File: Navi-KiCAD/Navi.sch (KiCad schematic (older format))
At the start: 30 parts, among them U10 Logo, U11 Logo, U6 LP5521YQ/NOPB

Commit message: Some BOM consolidation.
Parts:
- R40, R41: value DNP -> 0 DNP
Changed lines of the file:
@@
 U 1 1 58D60CF9
 P 2400 4400
-F 0 "R40" V 2450 4250 50  0000 C CNN
-F 1 "DNP" V 2400 4400 50  0000 C CNN
+F 0 "R40" V 2400 4400 50  0000 C CNN
+F 1 "0 DNP" V 2350 4150 50  0000 C CNN
 F 2 "Resistors_SMD:R_0402" V -5050 2750 50  0001 C CNN
 F 3 "" V -4770 2750 50  0001 C CNN
@@
 U 1 1 58D60FCF
 P 3450 4400
-F 0 "R41" V 3500 4600 50  0000 C CNN
-F 1 "DNP" V 3450 4400 50  0000 C CNN
+F 0 "R41" V 3450 4400 50  0000 C CNN
+F 1 "0 DNP" V 3500 4650 50  0000 C CNN
 F 2 "Resistors_SMD:R_0402" V -4000 2750 50  0001 C CNN
 F 3 "" V -3720 2750 50  0001 C CNN

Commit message: Completed key routing.
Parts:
- renumbered C91 to C1, C92 to C2, C93 to C3, C94 to C4, D3 to D1, D4 to D2, D8 to D3, R39 to R1, R28 to R10, R29 to R11, R30 to R12, R31 to R13, R32 to R14, R33 to R15, R34 to R16, R40 to R2, R24 to R3, R25 to R4, R26 to R5, R41 to R6, R45 to R7, R27 to R8, R49 to R9, U6 to U1, U10 to U2, U11 to U3
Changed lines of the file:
@@
 CPU-SDA
 $Comp
-L R R27
+L R R8
 U 1 1 58BFD165
 P 6400 2050
-F 0 "R27" H 6470 2149 50  0000 L CNN
+F 0 "R8" H 6470 2149 50  0000 L CNN
 F 1 "1k" H 6470 2058 50  0000 L CNN
 F 2 "Resistors_SMD:R_0402" V -1050 400 50  0001 C CNN
@@
 $EndComp
 $Comp
-L R R28
+L R R10
 U 1 1 58BFD565
 P 6650 2050
-F 0 "R28" H 6720 2149 50  0000 L CNN
+F 0 "R10" H 6720 2149 50  0000 L CNN
 F 1 "1k" H 6720 2058 50  0000 L CNN
 F 2 "Resistors_SMD:R_0402" V -800 400 50  0001 C CNN
@@
 $EndComp
 $Comp
-L R R26
+L R R5
 U 1 1 58C0DD41
 P 3400 4050
-F 0 "R26" V 3450 3850 50  0000 C CNN
+F 0 "R5" V 3450 3850 50  0000 C CNN
 F 1 "1k" V 3400 4050 50  0000 C CNN
 F 2 "Resistors_SMD:R_0402" V -4050 2400 50  0001 C CNN
@@
 $EndComp
 $Comp
-L R R25
+L R R4
 U 1 1 58C11226
 P 3400 3950
-F 0 "R25" V 3450 3750 50  0000 C CNN
+F 0 "R4" V 3450 3750 50  0000 C CNN
 F 1 "1k" V 3400 3950 50  0000 C CNN
 F 2 "Resistors_SMD:R_0402" V -4050 2300 50  0001 C CNN
@@
 $EndComp
 $Comp
-L R R24
+L R R3
 U 1 1 58C113C8
 P 3400 3850
-F 0 "R24" V 3450 3650 50  0000 C CNN
+F 0 "R3" V 3450 3650 50  0000 C CNN
 F 1 "1k" V 3400 3850 50  0000 C CNN
 F 2 "Resistors_SMD:R_0402" V -4050 2200 50  0001 C CNN
@@
 100k-PU
 $Comp
-L R R34
+L R R16
 U 1 1 58C4A4F7
 P 7850 4900
-F 0 "R34" V 7900 4700 50  0000 C CNN
+F 0 "R16" V 7900 4700 50  0000 C CNN
 F 1 "1k" V 7850 4900 50  0000 C CNN
 F 2 "Resistors_SMD:R_0402" V 400 3250 50  0001 C CNN
@@
 $EndComp
 $Comp
-L R R33
+L R R15
 U 1 1 58C4A502
 P 7850 4800
-F 0 "R33" V 7900 4600 50  0000 C CNN
+F 0 "R15" V 7900 4600 50  0000 C CNN
 F 1 "1k" V 7850 4800 50  0000 C CNN
 F 2 "Resistors_SMD:R_0402" V 400 3150 50  0001 C CNN
@@
 $EndComp
 $Comp
-L R R32
+L R R14
 U 1 1 58C4A50D
 P 7850 4700
-F 0 "R32" V 7900 4500 50  0000 C CNN
+F 0 "R14" V 7900 4500 50  0000 C CNN
 F 1 "1k" V 7850 4700 50  0000 C CNN
 F 2 "Resistors_SMD:R_0402" V 400 3050 50  0001 C CNN
@@
 100k-PU
 $Comp
-L R R31
+L R R13
 U 1 1 58C89A2C
 P 7850 3200
-F 0 "R31" V 7900 3000 50  0000 C CNN
+F 0 "R13" V 7900 3000 50  0000 C CNN
 F 1 "1k" V 7850 3200 50  0000 C CNN
 F 2 "Resistors_SMD:R_0402" V 400 1550 50  0001 C CNN
@@
 $EndComp
 $Comp
-L R R30
+L R R12
 U 1 1 58C89A37
 P 7850 3100
-F 0 "R30" V 7900 2900 50  0000 C CNN
+F 0 "R12" V 7900 2900 50  0000 C CNN
 F 1 "1k" V 7850 3100 50  0000 C CNN
 F 2 "Resistors_SMD:R_0402" V 400 1450 50  0001 C CNN
@@
 $EndComp
 $Comp
-L R R29
+L R R11
 U 1 1 58C89A42
 P 7850 3000
-F 0 "R29" V 7900 2800 50  0000 C CNN
+F 0 "R11" V 7900 2800 50  0000 C CNN
 F 1 "1k" V 7850 3000 50  0000 C CNN
 F 2 "Resistors_SMD:R_0402" V 400 1350 50  0001 C CNN
@@
 PD[0..11]
 $Comp
-L R R45
+L R R7
 U 1 1 58C46FCA
 P 5850 6700
-F 0 "R45" H 5920 6799 50  0000 L CNN
+F 0 "R7" H 5920 6799 50  0000 L CNN
 F 1 "10k" H 5920 6708 50  0000 L CNN
 F 2 "Resistors_SMD:R_0402" V -1600 5050 50  0001 C CNN
@@
 	5850 6950 5850 6850
 $Comp
-L LED D4
+L LED D2
 U 1 1 58C46FD1
 P 5850 7100
-F 0 "D4" V 5950 7050 50  0000 R CNN
+F 0 "D2" V 5950 7050 50  0000 R CNN
 F 1 "MF-LED-0603-GREEN" H 6100 7200 50  0000 R CNN
 F 2 "LEDs:LED_0603" H 450 750 50  0001 C CNN
@@
 $EndComp
 $Comp
-L LED D8
+L LED D3
 U 1 1 58C4B3ED
 P 6550 7100
-F 0 "D8" V 6650 7050 50  0000 R CNN
+F 0 "D3" V 6650 7050 50  0000 R CNN
 F 1 "MF-LED-0603-GREEN" H 6800 7200 50  0000 R CNN
 F 2 "LEDs:LED_0603" H 1150 750 50  0001 C CNN
@@
 $EndComp
 $Comp
-L R R49
+L R R9
 U 1 1 58C4B93C
 P 6550 6700
-F 0 "R49" H 6620 6799 50  0000 L CNN
+F 0 "R9" H 6620 6799 50  0000 L CNN
 F 1 "10k" H 6620 6708 50  0000 L CNN
 F 2 "Resistors_SMD:R_0402" V -900 5050 50  0001 C CNN
@@
 $EndComp
 $Comp
-L LED_BGR D3
+L LED_BGR D1
 U 1 1 58C9F1F2
 P 4850 6900
-F 0 "D3" V 4896 6570 50  0000 R CNN
+F 0 "D1" V 4896 6570 50  0000 R CNN
 F 1 "CLX6D-FKB-CMPQSGKBB7A363" H 5200 7300 50  0000 R CNN
 F 2 "LEDs:LED_PLCC6_3.4x3.4mm" H 200 150 50  0001 C CNN
@@
 $EndComp
 $Comp
-L C C91
+L C C1
 U 1 1 58CB9DB2
 P 1700 5650
-F 0 "C91" H 1750 5750 50  0000 L CNN
+F 0 "C1" H 1750 5750 50  0000 L CNN
 F 1 "1u" H 1750 5550 50  0000 L CNN
 F 2 "Capacitors_SMD:C_0402" H -4812 4350 50  0001 C CNN
@@
 $EndComp
 $Comp
-L C C94
+L C C4
 U 1 1 58CBBFFD
 P 3800 5650
-F 0 "C94" H 3850 5750 50  0000 L CNN
+F 0 "C4" H 3850 5750 50  0000 L CNN
 F 1 "1u" H 3850 5550 50  0000 L CNN
 F 2 "Capacitors_SMD:C_0402" H -2712 4350 50  0001 C CNN
@@
 	3450 5500 3800 5500
 $Comp
-L C C92
+L C C2
 U 1 1 58CBE629
 P 2500 5350
-F 0 "C92" V 2550 5450 50  0000 L CNN
+F 0 "C2" V 2550 5450 50  0000 L CNN
 F 1 "GRM155R61C474KE01D" V 2650 5100 50  0000 L CNN
 F 2 "Capacitors_SMD:C_0402" H -4012 4050 50  0001 C CNN
@@
 $EndComp
 $Comp
-L C C93
+L C C3
 U 1 1 58CBEC69
 P 3100 5350
-F 0 "C93" V 3150 5450 50  0000 L CNN
+F 0 "C3" V 3150 5450 50  0000 L CNN
 F 1 "GRM155R61C474KE01D" V 3250 4700 50  0000 L CNN
 F 2 "Capacitors_SMD:C_0402" H -3412 4050 50  0001 C CNN
@@
 	1200 5800 1200 6150
 $Comp
-L R R39
+L R R1
 U 1 1 58CCCAB3
 P 1200 5650
-F 0 "R39" H 1270 5749 50  0000 L CNN
+F 0 "R1" H 1270 5749 50  0000 L CNN
 F 1 "10k" H 1270 5658 50  0000 L CNN
 F 2 "Resistors_SMD:R_0402" V -6250 4000 50  0001 C CNN
@@
 	7050 4050 7550 4050
 $Comp
-L R R40
+L R R2
 U 1 1 58D60CF9
 P 2400 4400
-F 0 "R40" V 2400 4400 50  0000 C CNN
+F 0 "R2" V 2400 4400 50  0000 C CNN
 F 1 "0 DNP" V 2350 4150 50  0000 C CNN
 F 2 "Resistors_SMD:R_0402" V -5050 2750 50  0001 C CNN
@@
 $EndComp
 $Comp
-L R R41
+L R R6
 U 1 1 58D60FCF
 P 3450 4400
-F 0 "R41" V 3450 4400 50  0000 C CNN
+F 0 "R6" V 3450 4400 50  0000 C CNN
 F 1 "0 DNP" V 3500 4650 50  0000 C CNN
 F 2 "Resistors_SMD:R_0402" V -4000 2750 50  0001 C CNN
@@
 CPU-SDA
 $Comp
-L BOX1 U11
+L BOX1 U3
 U 1 1 58D75525
 P 7900 6300
-F 0 "U11" H 7950 6350 50  0001 C CNN
+F 0 "U3" H 7950 6350 50  0001 C CNN
 F 1 "Logo" H 8028 6300 50  0000 L CNN
 F 2 "Symbols:NaviLOGO" H 1550 850 60  0001 C CNN
@@
 $EndComp
 $Comp
-L BOX1 U10
+L BOX1 U2
 U 1 1 58D772A7
 P 7900 6150
-F 0 "U10" H 7950 6200 50  0001 C CNN
+F 0 "U2" H 7950 6200 50  0001 C CNN
 F 1 "Logo" H 8028 6150 50  0000 L CNN
 F 2 "Symbols:NaviLOGO" H 1550 700 60  0001 C CNN
@@
 $EndComp
 $Comp
-L LP5521YQ U6
+L LP5521YQ U1
 U 1 1 58D0B021
 P 2800 6450
-F 0 "U6" H 2100 5650 60  0000 C CNN
+F 0 "U1" H 2100 5650 60  0000 C CNN
 F 1 "LP5521YQ/NOPB" H 3250 5650 60  0000 C CNN
 F 2 "Housings_DFN_QFN:QFN-24-1EP_4x5mm_Pitch0.5mm" H -150 -800 60  0001 C CNN

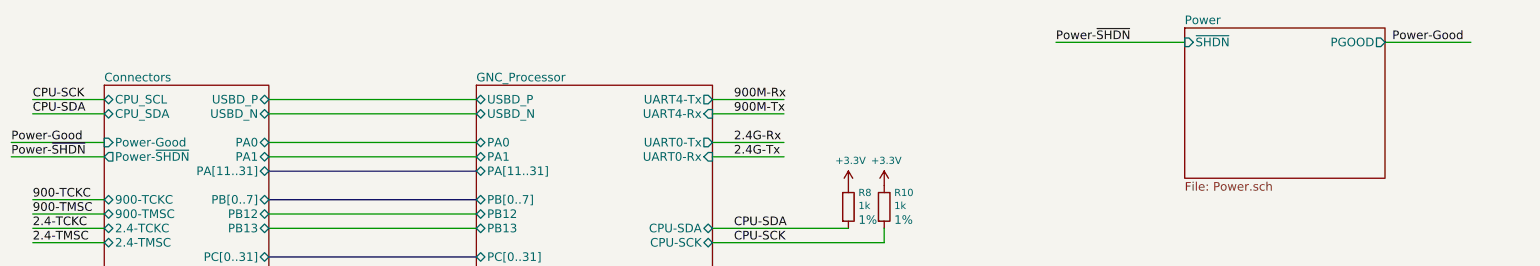
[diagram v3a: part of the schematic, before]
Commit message: Additional routing
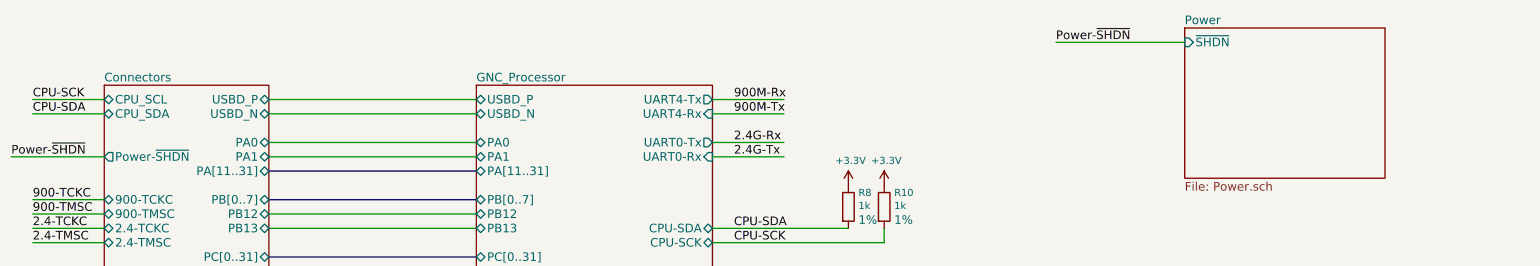
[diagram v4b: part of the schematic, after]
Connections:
- net labels removed: Power-Good
- wire segments 119 -> 117
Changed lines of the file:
@@
 F1 "Power.sch" 60
 F2 "~SHDN" I L 8750 900 60
-F3 "PGOOD" O R 10150 900 60
 $EndSheet
 $Sheet
@@
 F29 "2.4-DIO-[7..22]" B R 2350 3400 60
 F30 "2.4-ADIO-[23..30]" B R 2350 3500 60
-F31 "Power-Good" I L 1200 1600 60
-F32 "Power-~SHDN" O L 1200 1700 60
+F31 "Power-~SHDN" O L 1200 1700 60
 $EndSheet
 Text Label 5600 1600 0    60   ~ 0
@@
 Power-~SHDN~
 Wire Wire Line
-	10150 900  10750 900
-Text Label 10200 900  0    60   ~ 0
-Power-Good
-Wire Wire Line
 	1200 1700 550  1700
 Text Label 550  1700 0    60   ~ 0
 Power-~SHDN~
 Wire Wire Line
-	550  1600 1200 1600
-Text Label 550  1600 0    60   ~ 0
-Power-Good
-Wire Wire Line
 	3800 2900 2350 2900

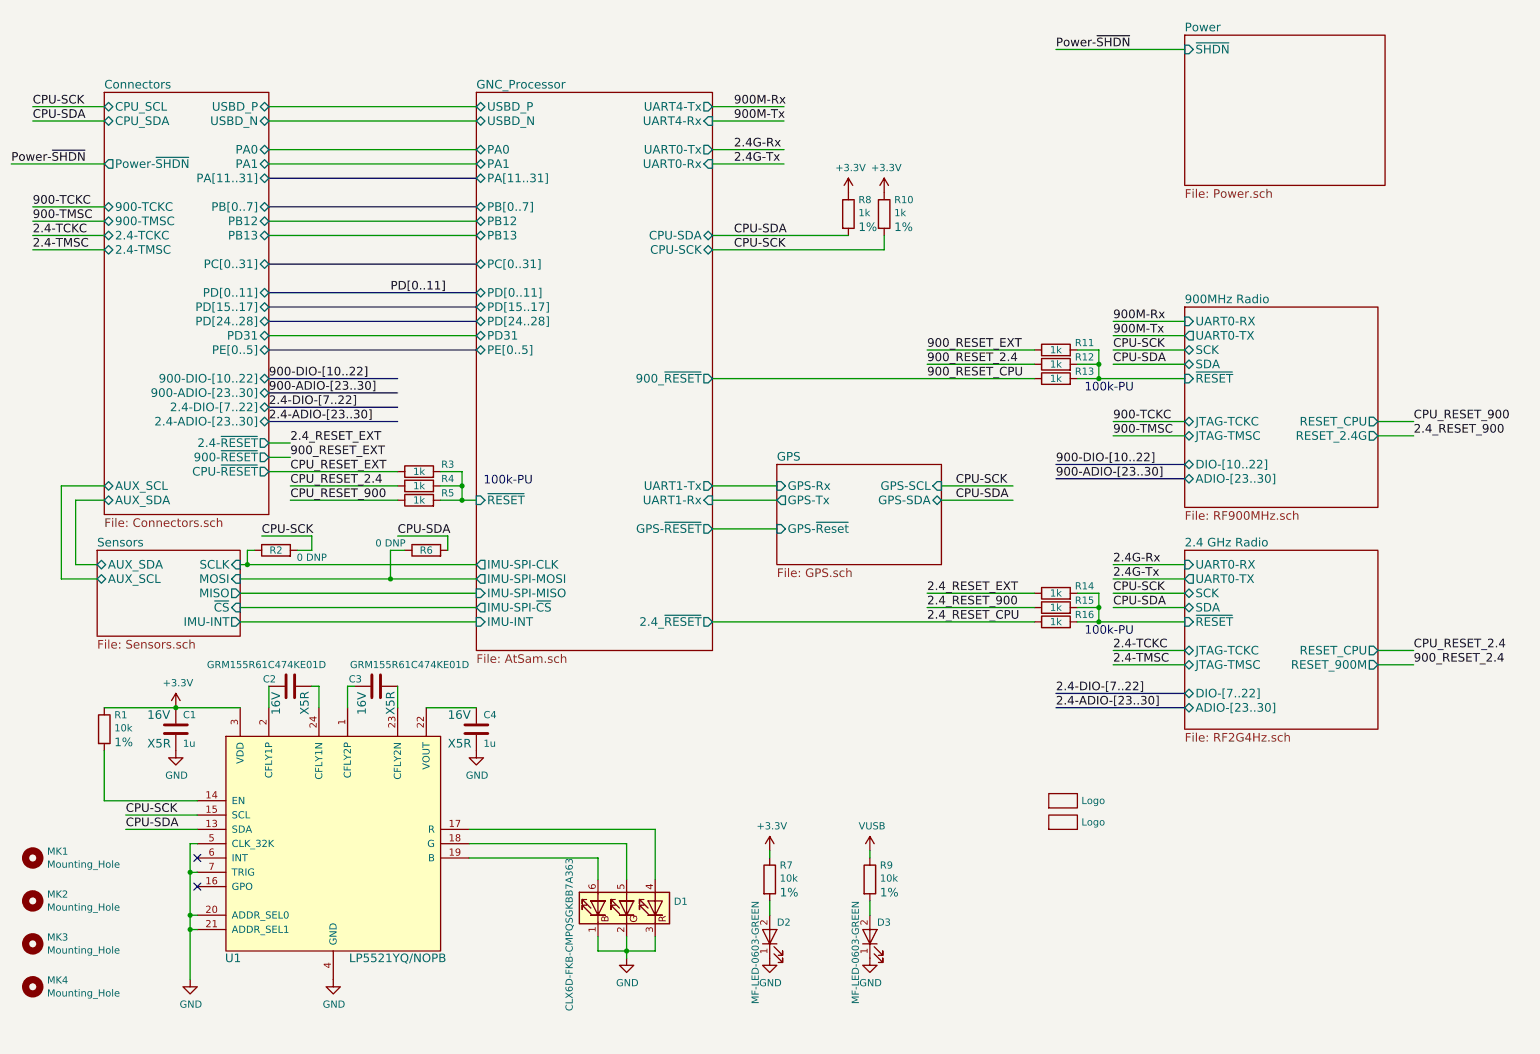
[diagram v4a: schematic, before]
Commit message: Upgraded to 9 channel RGB driver. Broke out signals for LSM303 and LSM6DS3
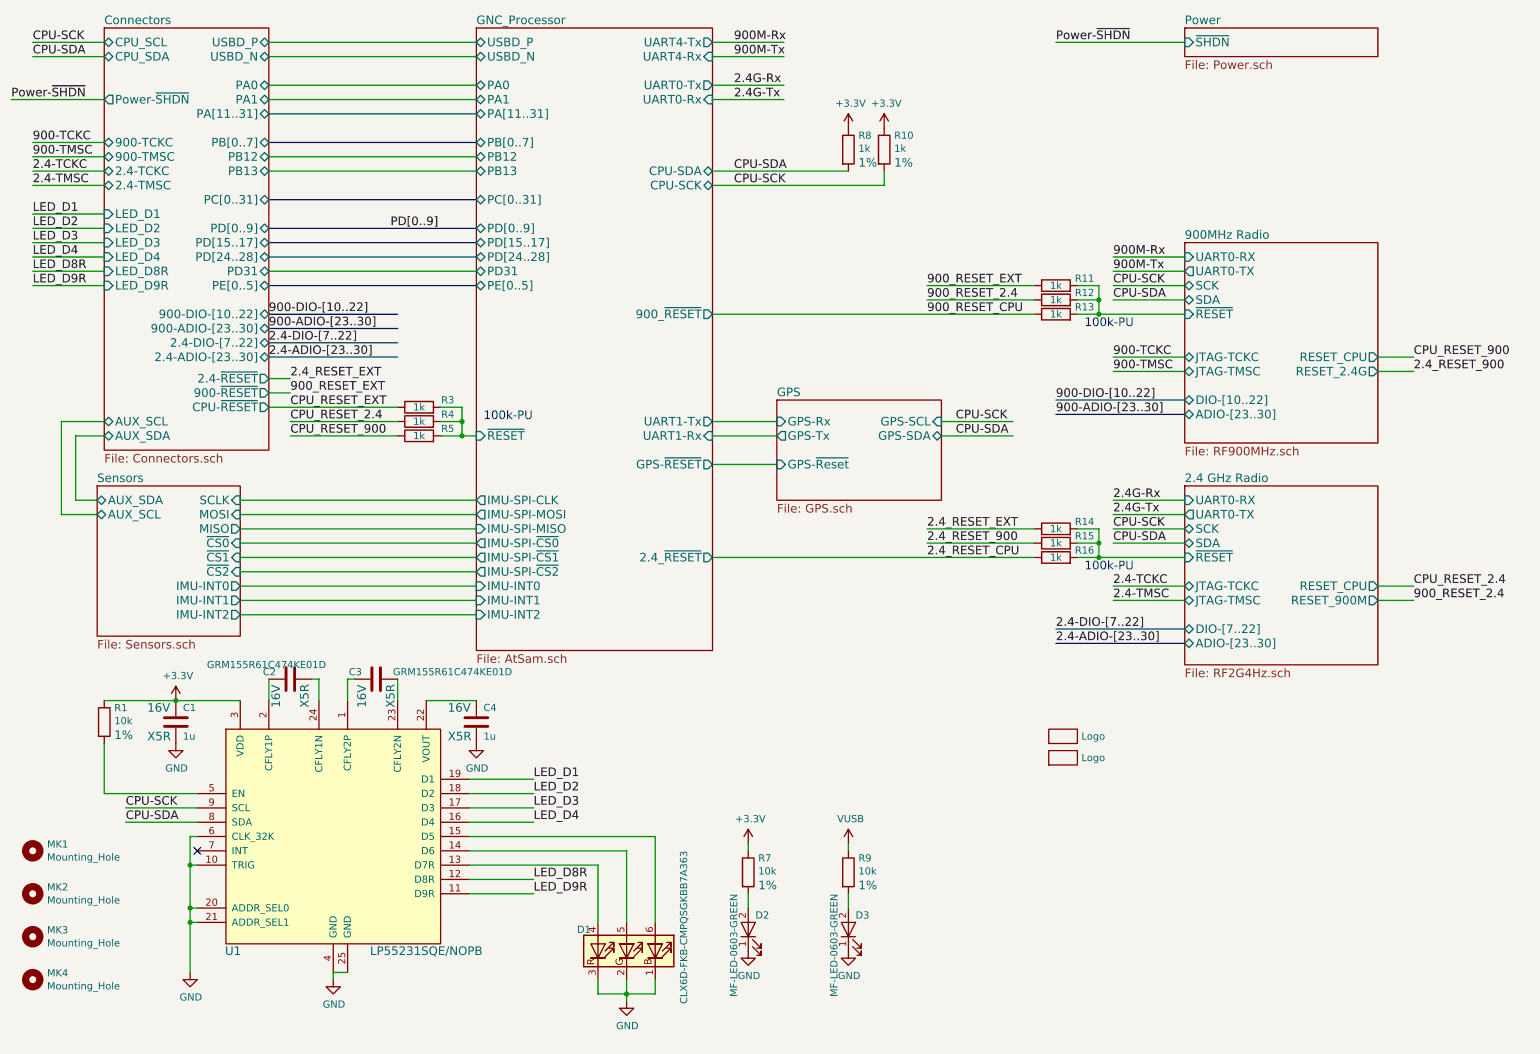
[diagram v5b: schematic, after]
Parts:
- removed R2, R6: 0 DNP, Resistors_SMD:R_0402, symbol R
- removed U1: LP5521YQ/NOPB, Housings_DFN_QFN:QFN-24-1EP_4x5mm_Pitch0.5mm, symbol LP5521YQ
- added U1: LP55231SQE/NOPB, Housings_DFN_QFN:QFN-24-1EP_4x4mm_Pitch0.5mm, symbol LP55231SQE/NOPB
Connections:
- net labels added: LED_D1, LED_D2, LED_D3, LED_D4, LED_D8R, LED_D9R, PD[0..9]
- net labels removed: PD[0..11]
- wire segments 117 -> 126
- no-connect marks 2 -> 1
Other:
- moved on the sheet: C1, C2, C3, C4, D1, D2, D3, MK1, MK2, MK3, MK4, R1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

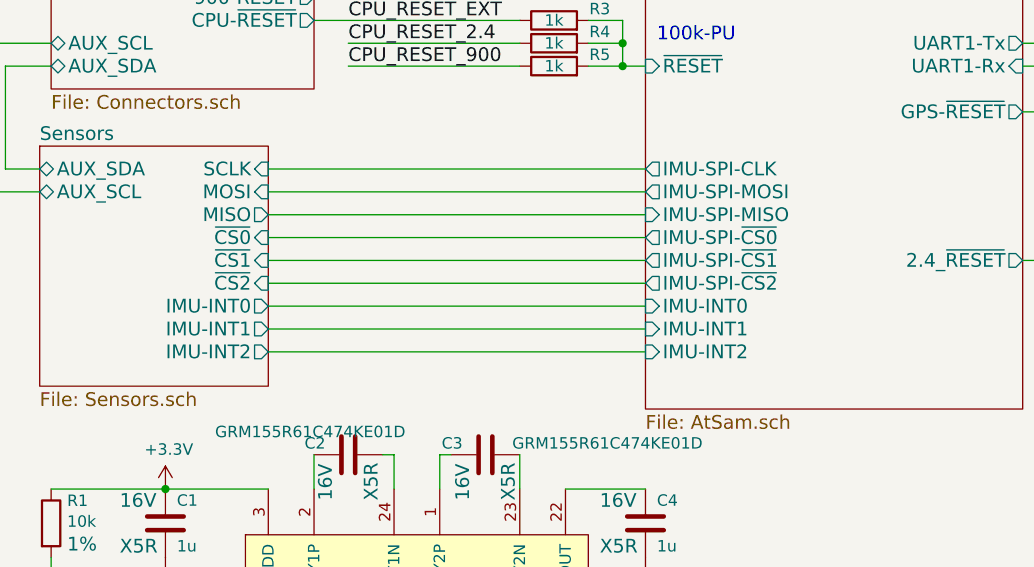
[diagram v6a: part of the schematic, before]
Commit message: Finished reroute
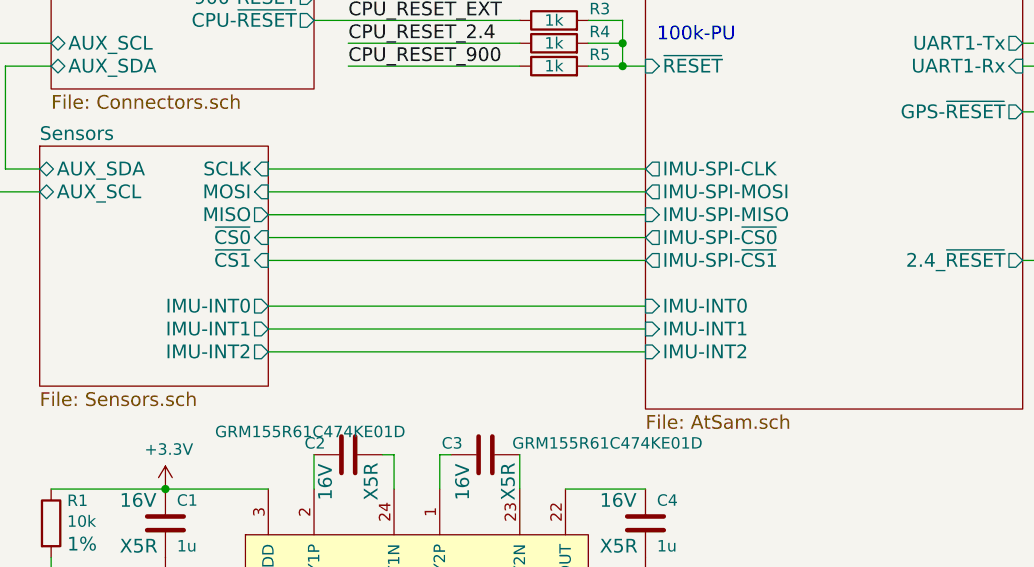
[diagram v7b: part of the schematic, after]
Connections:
- wire segments 126 -> 125
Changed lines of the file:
@@
 F10 "~CS1" I R 2150 4450 60
 F11 "IMU-INT2" O R 2150 4850 60
-F12 "~CS2" I R 2150 4550 60
 $EndSheet
 $Sheet
@@
 F31 "IMU-SPI-~CS0" O L 3800 4350 60
 F32 "IMU-SPI-~CS1" O L 3800 4450 60
-F33 "IMU-SPI-~CS2" O L 3800 4550 60
-F34 "IMU-INT0" I L 3800 4650 60
-F35 "IMU-INT1" I L 3800 4750 60
-F36 "IMU-INT2" I L 3800 4850 60
+F33 "IMU-INT0" I L 3800 4650 60
+F34 "IMU-INT1" I L 3800 4750 60
+F35 "IMU-INT2" I L 3800 4850 60
 $EndSheet
 Wire Wire Line
-	2150 4550 3800 4550
-Wire Wire Line
 	3800 4650 2150 4650
